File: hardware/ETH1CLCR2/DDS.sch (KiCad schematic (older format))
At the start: 90 parts, among them Q1201 FDV301N, U1201 LMH6639MA, U1202 AD9834, U1203 AD8038ARZ, U1204 DAC7811, U1205 AD8038ARZ, U1206 DG409DY, U1207 LMH6639MA, U1208 SN74LVC1T45DBV, U1209 74AHC1G14, U1210 74AUP1G79, U1211 SN74LVC1T45DBV, U1212 74AC161, U1213 74AC161, U1214 SN74LVC1T45DBV, X1201 830208220601

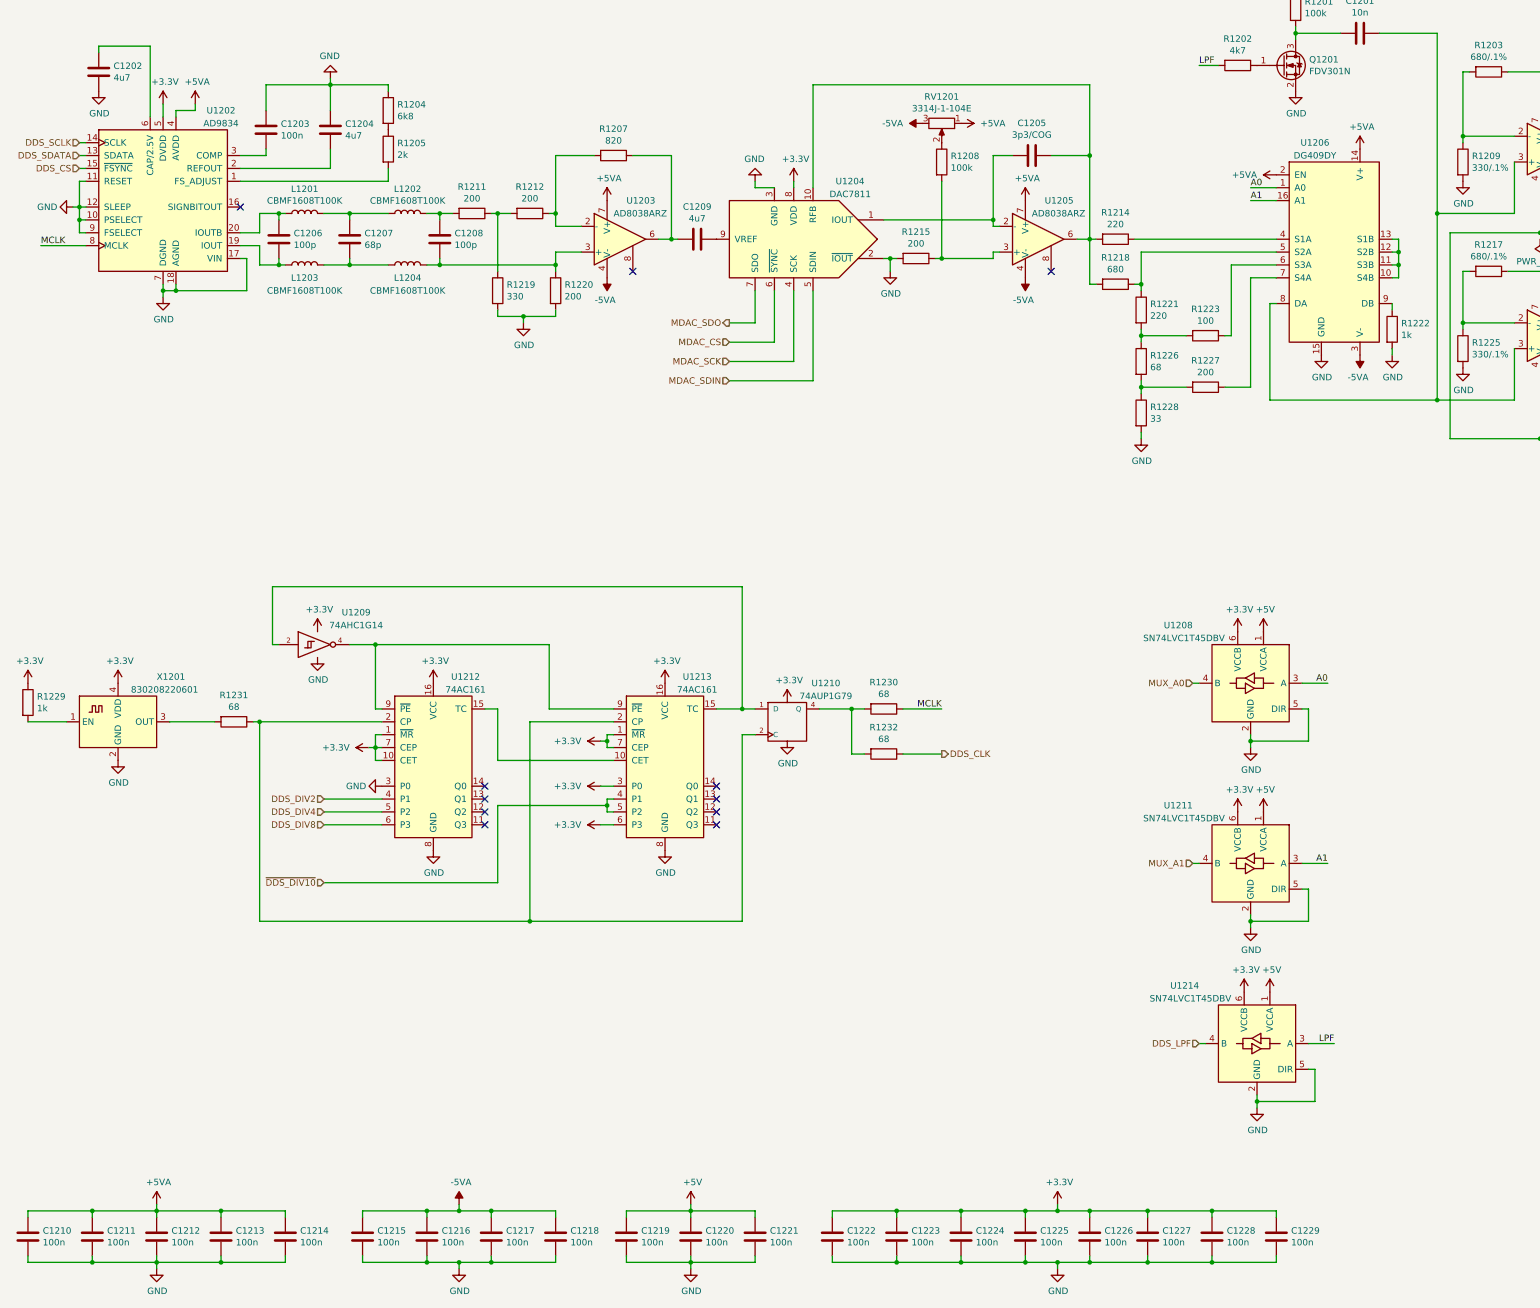
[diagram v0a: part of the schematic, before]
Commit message: Modification in schematic and PCB
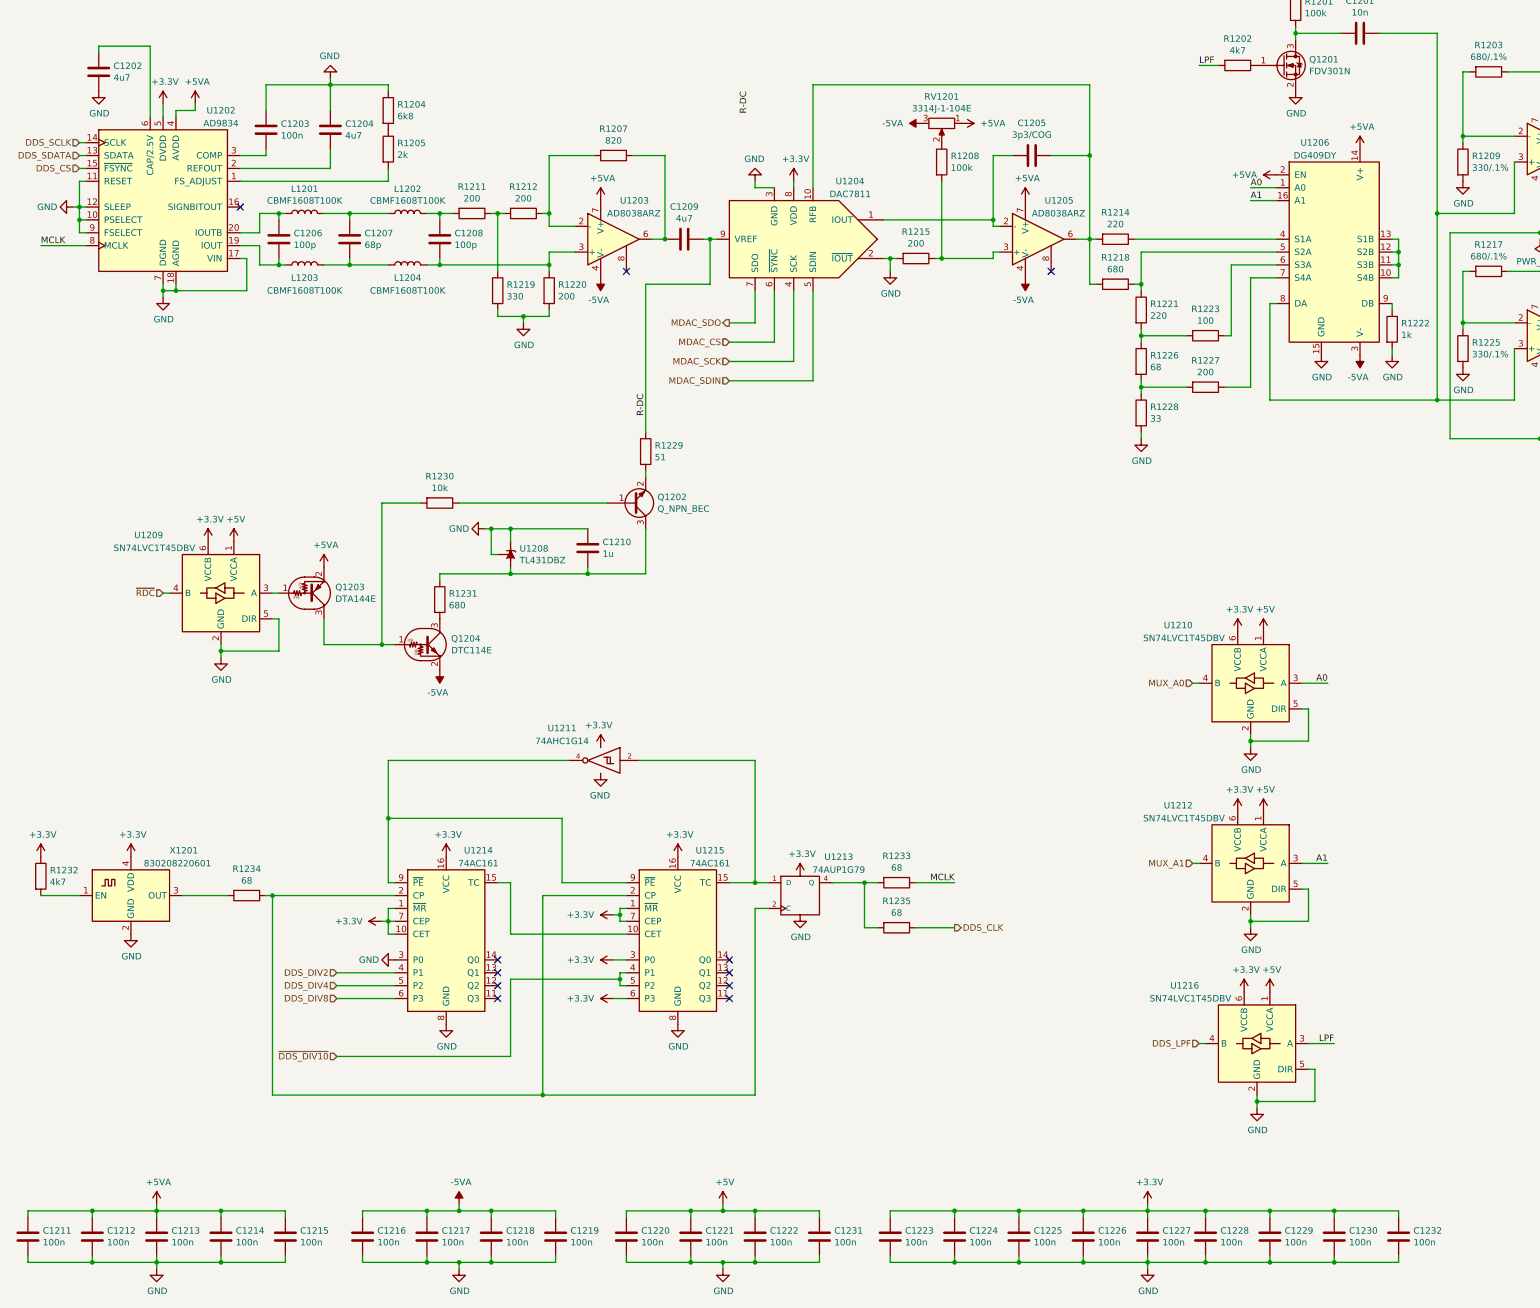
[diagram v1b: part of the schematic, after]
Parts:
- added C1210: 1u, Capacitor_SMD:C_0603_1608Metric_Pad1.08x0.95mm_HandSolder, symbol Device:C
- added C1231, C1232: 100n, Capacitor_SMD:C_0603_1608Metric_Pad1.08x0.95mm_HandSolder, symbol Device:C
- added Q1202: Q_NPN_BEC, Package_TO_SOT_SMD:SOT-23, symbol Device:Q_NPN_BEC
- added Q1203: DTA144E, Package_TO_SOT_SMD:SOT-23, symbol Transistor_BJT:DTA144E
- added Q1204: DTC114E, Package_TO_SOT_SMD:SOT-23, symbol Transistor_BJT:DTC114E
- added R1229: 51, Resistor_SMD:R_0603_1608Metric_Pad0.98x0.95mm_HandSolder, symbol Device:R
- added R1230: 10k, Resistor_SMD:R_0603_1608Metric_Pad0.98x0.95mm_HandSolder, symbol Device:R
- added R1231: 680, Resistor_SMD:R_0603_1608Metric_Pad0.98x0.95mm_HandSolder, symbol Device:R
- added U1208: TL431DBZ, Package_TO_SOT_SMD:SOT-23, symbol Reference_Voltage:TL431DBZ
- added U1209: SN74LVC1T45DBV, Package_TO_SOT_SMD:SOT-23-6, symbol Logic_LevelTranslator:SN74LVC1T45DBV
- R1232: renamed from R1229; value 1k -> 4k7
- renumbered C1210 to C1211, C1211 to C1212, C1212 to C1213, C1213 to C1214, C1214 to C1215, C1215 to C1216, C1216 to C1217, C1217 to C1218, C1218 to C1219, C1219 to C1220, C1220 to C1221, C1221 to C1222, C1222 to C1223, C1223 to C1224, C1224 to C1225, C1225 to C1226, C1226 to C1227, C1227 to C1228, C1228 to C1229, C1229 to C1230, R1230 to R1233, R1231 to R1234, R1232 to R1235, U1208 to U1210, U1209 to U1211, U1211 to U1212, U1210 to U1213, U1212 to U1214, U1213 to U1215, U1214 to U1216
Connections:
- net +3V3: now also C1232.1, U1209.6 (VCCB)
- net +5V: now also C1231.1, U1209.1 (VCCA)
- net +5VA: now also Q1203.2 (E)
- net -5VA: now also Q1204.2 (E)
- net GND: now also C1210.1, C1231.2, C1232.2, U1208.1 (K), U1208.2 (REF), U1209.2 (GND), U1209.5 (DIR)
- net R-DC: now reaches C1209.1, U1204.9 (VREF)
- net R-DC: now also R1229.1
- new net: Q1203.1 (B), U1209.3 (A)
- new net: Q1203.3 (C), Q1204.1 (B), R1230.2
- new net: Q1204.3 (C), R1231.2
- new net: C1210.2, Q1202.3 (C), R1231.1, U1208.3 (A)
- new net: Q1202.1 (B), R1230.1
- new net: Q1202.2 (E), R1229.2
- new net ~RDC: U1209.4 (B)
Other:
- moved on the sheet: C1209, C1223, C1224, C1225, C1226, C1227, C1228, C1229, C1230, R1212, R1220, R1232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
